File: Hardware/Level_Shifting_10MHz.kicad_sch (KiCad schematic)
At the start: 32 parts, among them J8 SMA_Edge, SW5 DPDT_Slide_SMD_7.2x3.5mm, U14 74LVC2T45DC, U15 74LVC2T45DC, U17 LMV7219M5

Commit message: Add jumpers for 2.8V and 1.8V In / Out
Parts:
- added R.1: ~, SparkFun-Jumper:Jumper_2_NC_Trace, symbol SparkFun-Jumper:SolderJumper_2_Bridged
- added S.1, T.1: ~, SparkFun-Jumper:Jumper_2_NO, symbol SparkFun-Jumper:SolderJumper_2_Open
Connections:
- net 1.8V: now also T.1.2 (B)
- net 2.8V: now also S.1.2 (B)
- net VCCIO: now also R.1.2 (B); no longer C49.1, C51.1, U15.8 (VCCB)
- new net: C49.1, C51.1, R.1.1 (A), S.1.1 (A), T.1.1 (A), U15.8 (VCCB)
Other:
- note added: "For 2.8V output: Open jumper R Close jumper S For 1.8V output: Open jumper R Close jumper T"
- moved on the sheet: A.1, B.1, C.1, C24, C49, C50, C51, D.1, R46, R49, U15

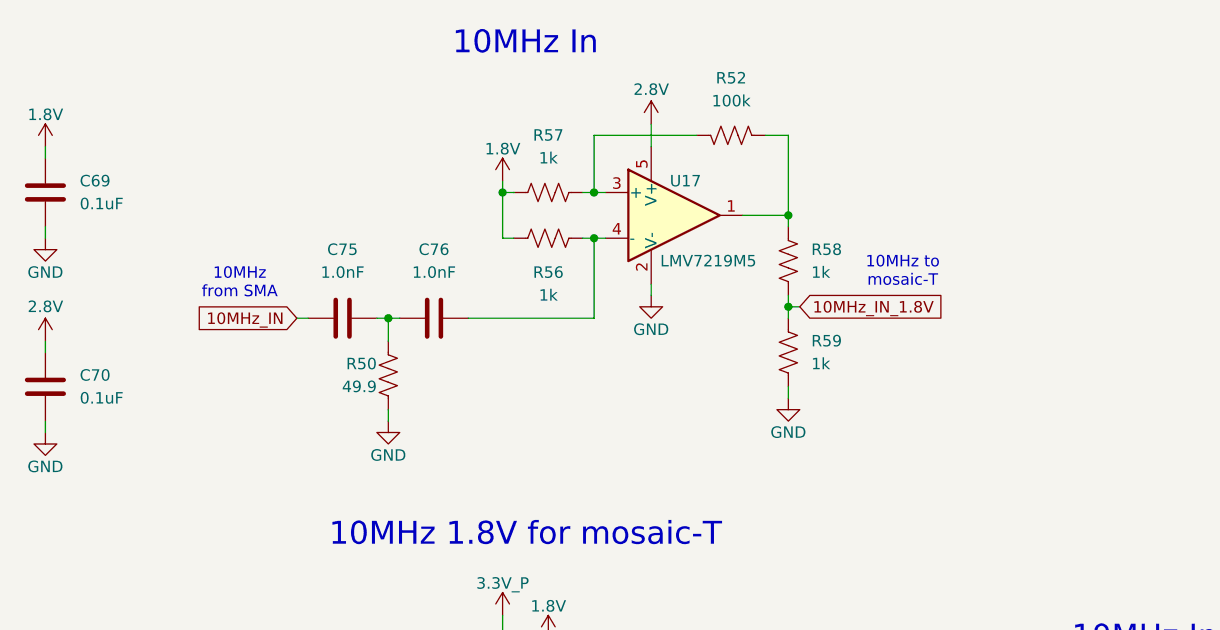
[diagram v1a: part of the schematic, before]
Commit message: Add mounting holes for SiT5811 / Rakon oscillator
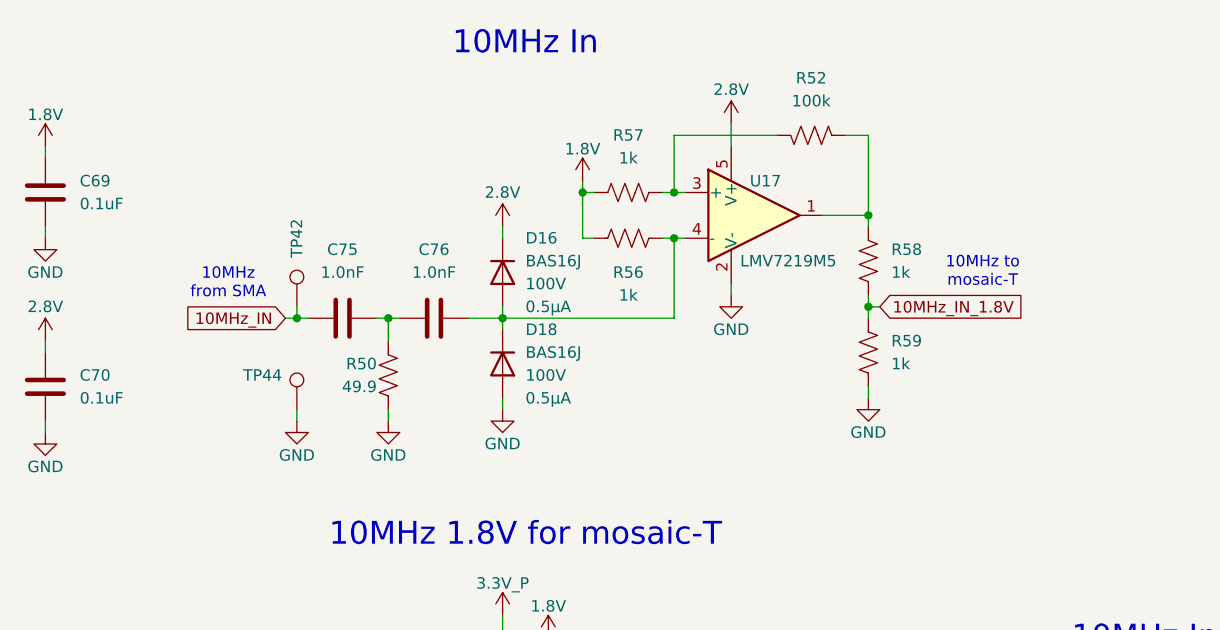
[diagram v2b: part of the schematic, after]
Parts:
- added D16, D18: BAS16J, SparkFun-Semiconductor-Standard:SOD-323, symbol SparkFun-DiscreteSemi:D_250mA_100V
- added TP42, TP44: PTH, SparkFun-Connector:1x01, symbol SparkFun-Connector:TestPoint_PTH
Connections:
- net 10MHz_IN: now also TP42.1
- net 2.8V: now also D16.C
- net GND: now also D18.A, TP44.1
- net at C76.2, R56.2, U17.4 (-): now also D16.A, D18.C
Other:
- moved on the sheet: R52, R56, R57, R58, R59, U17

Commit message: Final changes before name change
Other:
- note added: "10MHz In Input impedance: 50Ω Detection level: -14dBm Max supported level: +12dBm"
- note removed: "10MHz In"
- moved on the sheet: A.1, B.1, C.1, C24, C49, C50, C51, C52, C55, C68, C69, C70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
